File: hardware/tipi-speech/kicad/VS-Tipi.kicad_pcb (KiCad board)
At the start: 2 copper layers, 115.7 x 54.7 mm, 32 parts, among them J1 TI-99_Sideport, J2 USB_B_Micro, P1 TI-99_Sideport, Q1 NPN_BCE, U1 XC95144XL-TQ100, U2 27C256, U3 74HCT245, U4 LM1117-3.3, U5 CY62256L-70PC

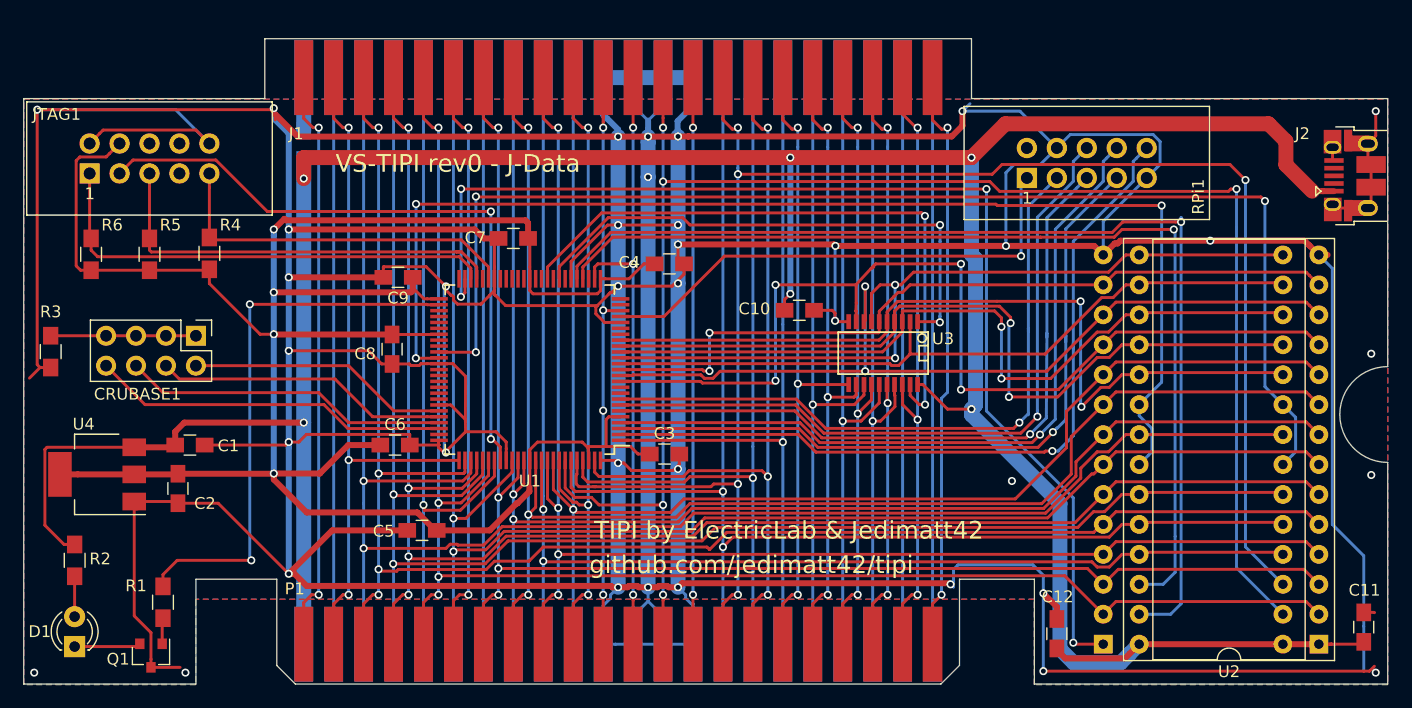
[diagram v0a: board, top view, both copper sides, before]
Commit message: TIPI-32K V1 HW and CPLD update
V1 hardware and CPLD updates to add power tap and make RAM disableable.
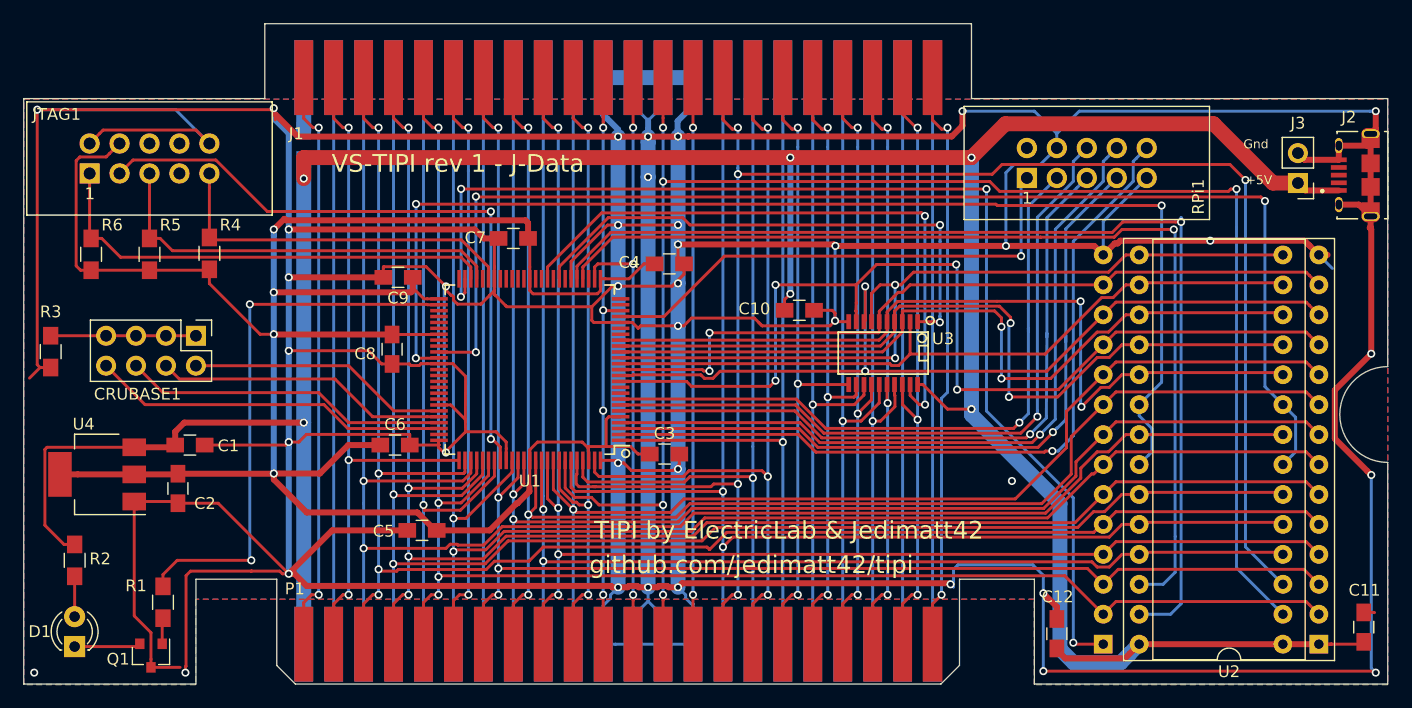
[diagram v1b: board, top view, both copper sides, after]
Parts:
- added J3: Conn_01x02, Connector_PinHeader_2.54mm:PinHeader_1x02_P2.54mm_Vertical, F.Cu at (168.9, 102.7)
- J2: footprint Connector_USB:USB_Micro-B_Amphenol_10103594-0001LF_Horizontal -> VS-TIPI-kicad:AMPHENOL_10118194-0001LF
- moved J2 1.34 mm to (175.1, 102.0)
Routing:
- net GND: track 828.7 -> 895.9 mm, vias 38 -> 39
- net +5V: track 272.8 -> 271.7 mm
- net JTAG_TMS: track 36.1 -> 35.3 mm
- net JTAG_TCK: track 40.3 -> 39.8 mm
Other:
- board size 115.7 x 54.7 mm -> 115.7 x 56 mm
- rule trace_min: 0.1524 -> 0.2286
- board text added: "+5V"
- board text added: "Gnd"
- board text added: "VS-TIPI rev 1 - J-Data"
- board text removed: "VS-TIPI rev0 - J-Data"
